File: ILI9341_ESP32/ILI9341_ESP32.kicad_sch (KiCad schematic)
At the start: 65 parts, among them J1 USB_C_Receptacle_USB2.0_16P, J10 Conn_01x01_Pin, J9 Conn_01x01_Pin, Q1 BC817, Q10 PMOS, Q4 BC817, Q9 BC817, SW1 SS-12F23-G040, U1 TPS61028DRCR, U10 CH340K, U2 XM5062S, U7 02FVS3, U9 BQ25171QWDRCRQ1

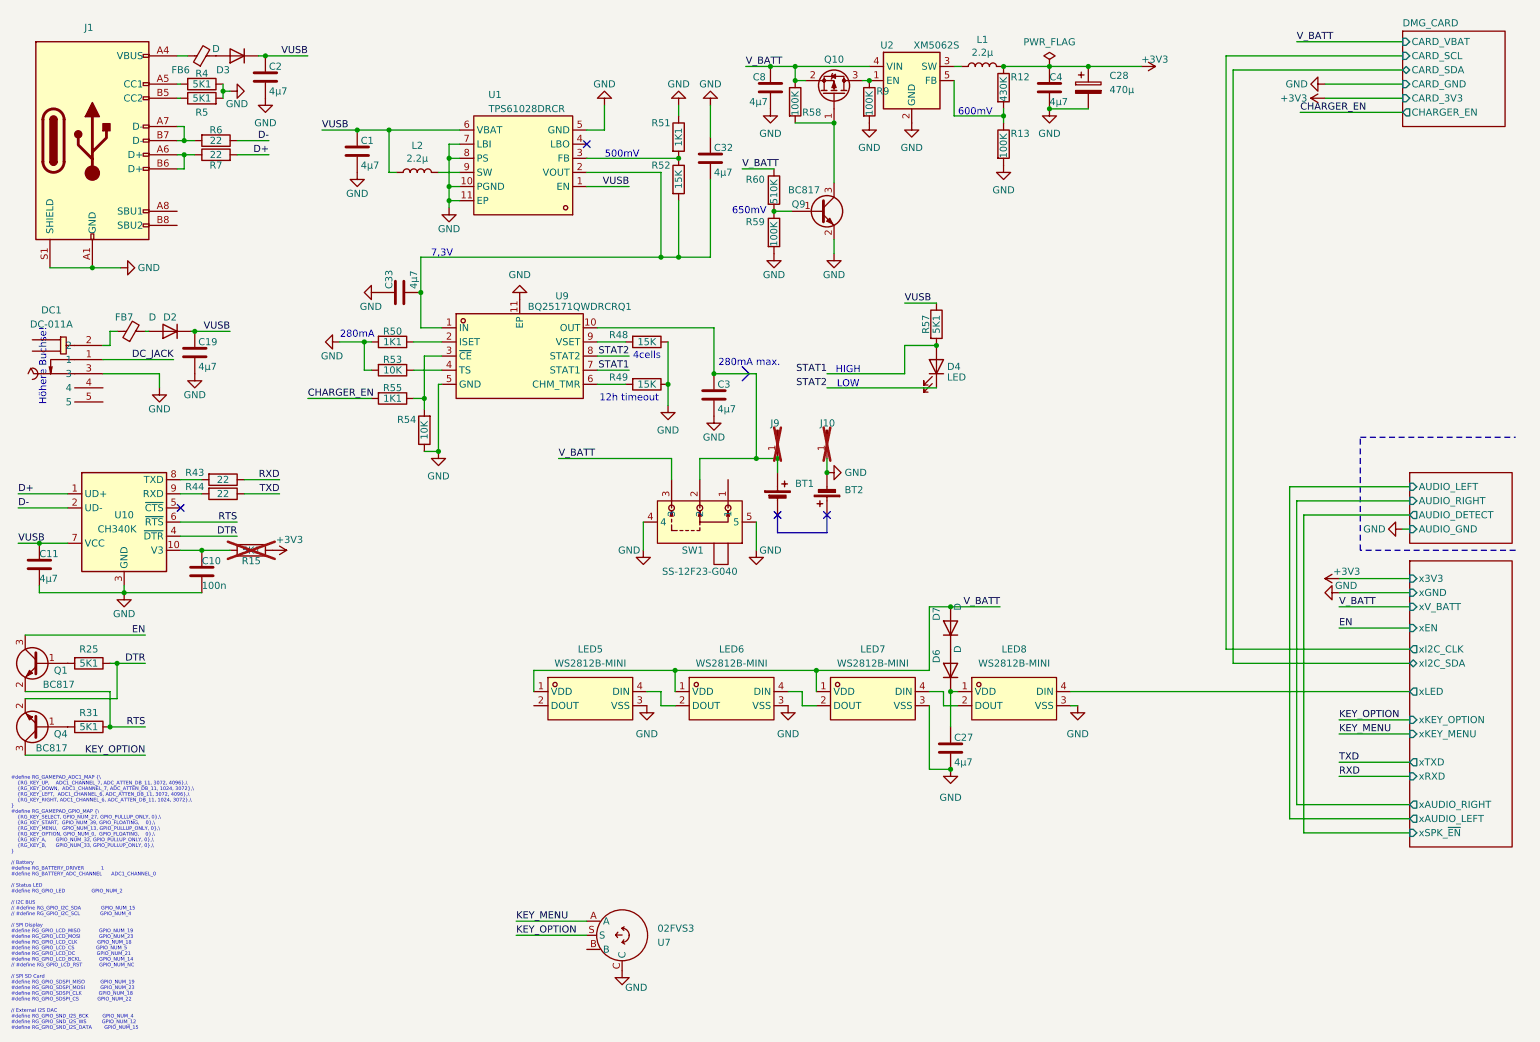
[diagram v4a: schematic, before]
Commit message: upload new untested version
the boosconverter should work now :)
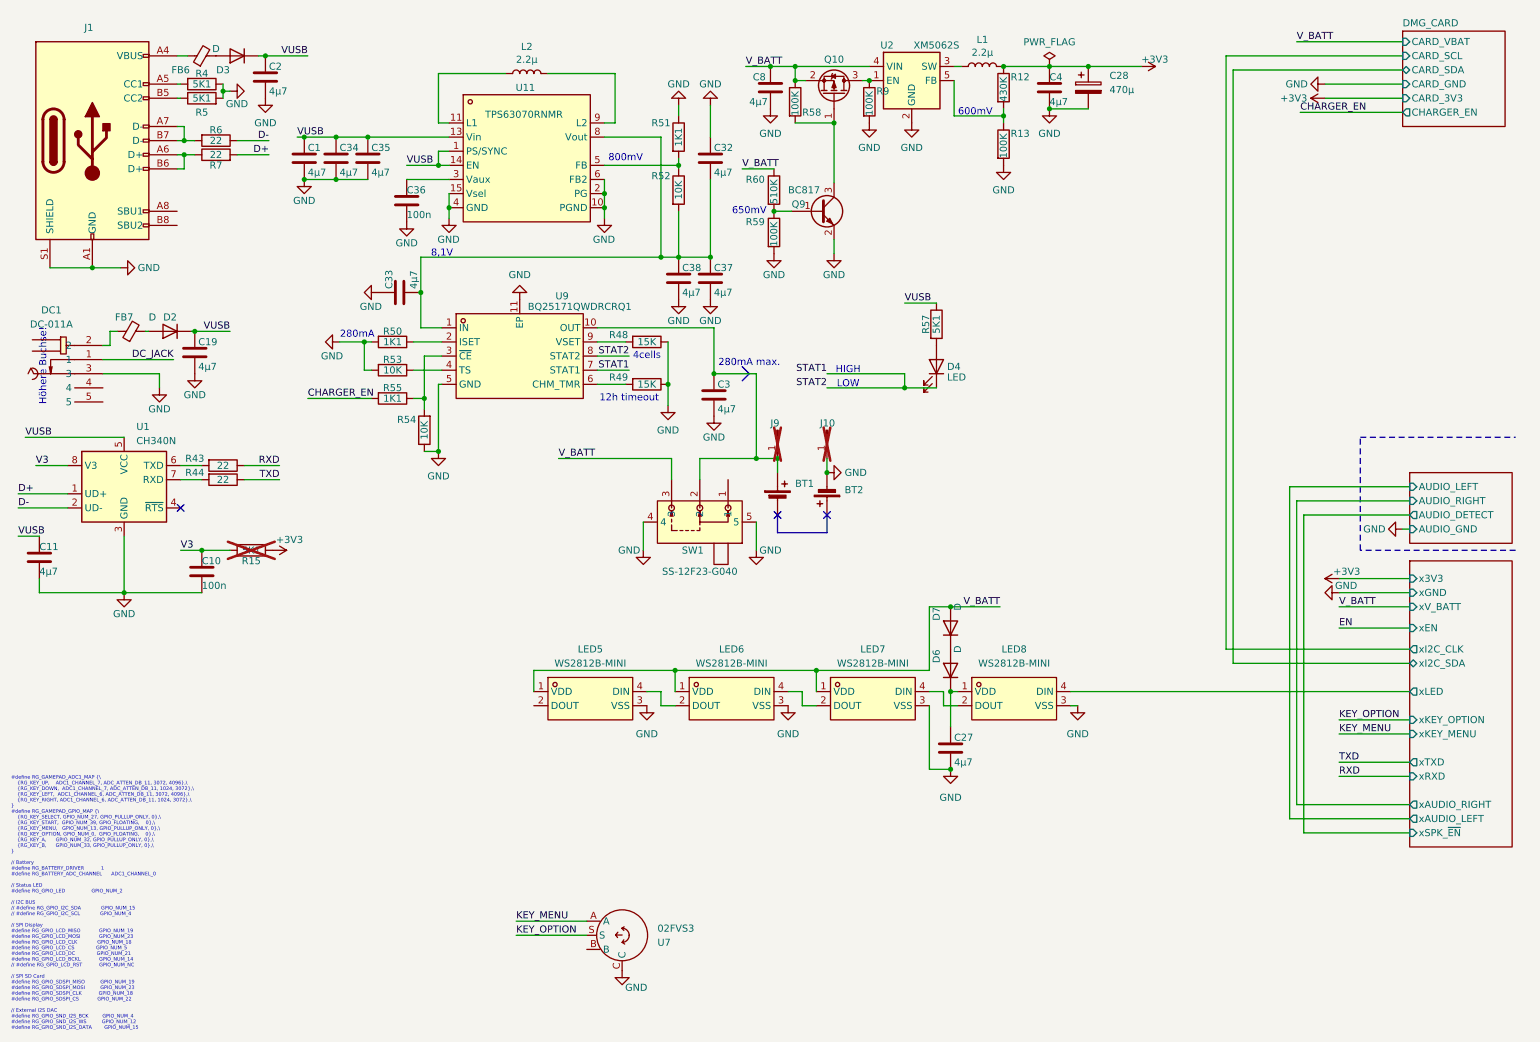
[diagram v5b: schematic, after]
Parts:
- removed Q1, Q4: BC817, Package_TO_SOT_SMD:SOT-323_SC-70, symbol Transistor_BJT:BC817
- removed R25, R31: 5K1, Resistor_SMD:R_0603_1608Metric, symbol Device:R
- removed U1: TPS61028DRCR, easyeda2kicad:VSON-10_L3.0-W3.0-P0.50-TL-EP-1, symbol easyeda2kicad:TPS61028DRCR
- removed U10: CH340K, TheBrutzlers_Lib:SSOP-10_3.9x4.9mm_P1.00mm_EP_3mmx2mm, symbol theBrutzler:CH340K
- added C34, C35, C37, C38: 4µ7, Capacitor_SMD:C_1206_3216Metric, symbol Device:C
- added C36: 100n, Capacitor_SMD:C_0603_1608Metric, symbol Device:C
- added U1: CH340N, Package_SO:SOP-8_3.9x4.9mm_P1.27mm, symbol Interface_USB:CH340N
- added U11: TPS63070RNMR, easyeda2kicad:VQFN-HR-15_L3.0-W2.5-P0.50-BL_TPS63070RNMR, symbol easyeda2kicad:TPS63070RNMR
- R52: value 15K -> 10K; LCSC C2906995 -> C25804
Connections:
- net STAT2 is gone; now on net STAT1: D4.1 (K), U9.8 (STAT2)
- net D+: now also U1.1 (UD+)
- net D-: now also U1.2 (UD-)
- net GND: now also C34.2, C35.2, C36.2, C37.2, C38.2, U1.3 (GND), U11.10 (PGND), U11.15 (Vsel), U11.2 (PG), U11.4 (GND), U11.6 (FB2)
- net STAT1: no longer D4.2 (A), R57.2
- net VUSB: now also C34.1, C35.1, U1.5 (VCC), U11.1 (PS/SYNC), U11.12 (Vin), U11.13 (Vin), U11.14 (EN); no longer L2.1
- net at R44.2: now also U1.7 (RXD)
- net at C32.2, C33.2, R52.2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: now also C37.1, C38.1, U11.7 (Vout), U11.8 (Vout)
- net at R51.2, R52.1: now also U11.5 (FB)
- net at L2.2: now also U11.9 (L2)
- net at R43.2: now also U1.6 (TXD)
- net V3: now reaches C10.1, R15.1
- net V3: now also U1.8 (V3)
- new net: D4.2 (A), R57.2
- new net: C36.1, U11.3 (Vaux)
- new net: L2.1, U11.11 (L1)
- no-connect marks 4 -> 3
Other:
- note added: "8,1V"
- note added: "800mV"
- note removed: "500mV"
- note removed: "7,3V"
- moved on the sheet: C1, C11, L2, R43, R44, R52
